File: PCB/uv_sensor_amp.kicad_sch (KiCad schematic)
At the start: 4 parts, among them U2 LMV321

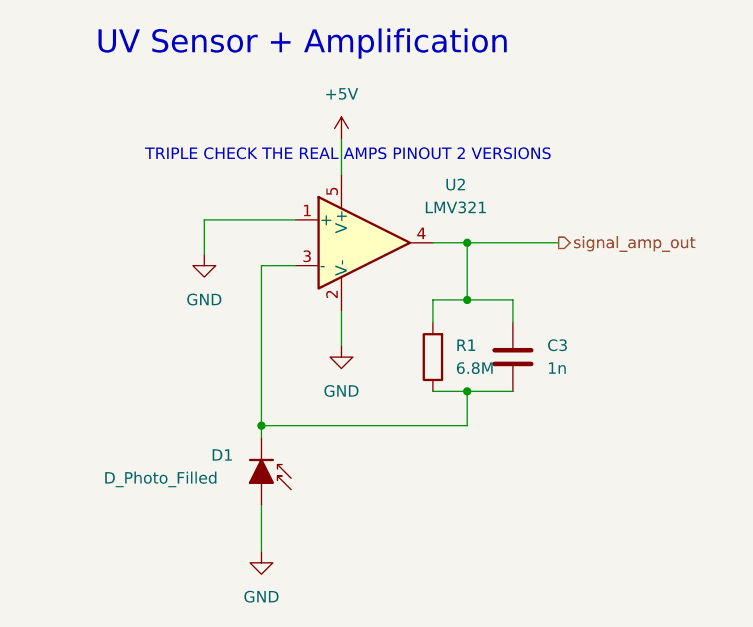
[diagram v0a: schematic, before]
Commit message: add footprints for power supply
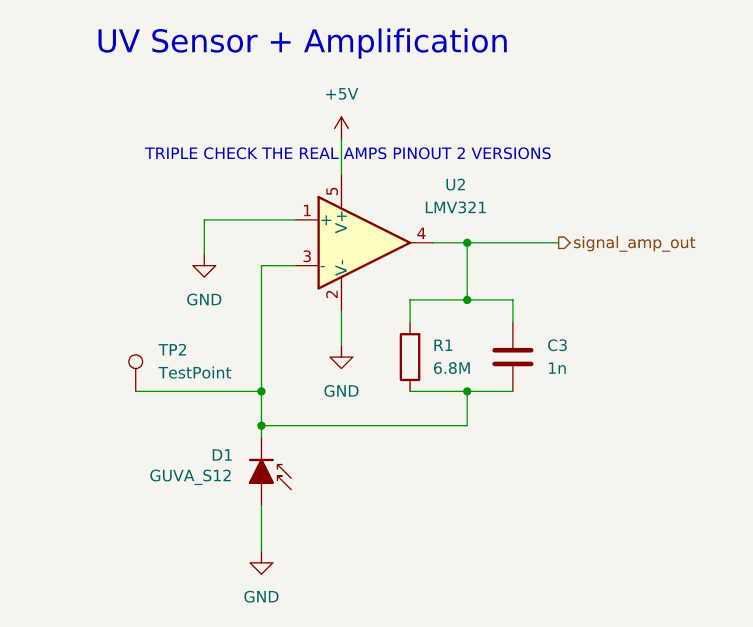
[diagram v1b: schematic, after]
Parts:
- added TP2: TestPoint, TestPoint:TestPoint_Keystone_5000-5004_Miniature, symbol Connector:TestPoint
- D1: value D_Photo_Filled -> GUVA_S12
- R1: footprint Resistor_SMD:R_0402_1005Metric -> Resistor_SMD:R_0805_2012Metric_Pad1.20x1.40mm_HandSolder
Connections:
- net at C3.2, D1.1 (K), R1.1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: now also TP2.1
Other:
- moved on the sheet: R1
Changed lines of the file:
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@@
 		(color 0 0 0 0)
 	)
+	(junction
+		(at 113.03 92.71)
+		(diameter 0)
+		(color 0 0 0 0)
+	)
 	(wire
 		(pts
@@
 	(wire
 		(pts
+			(xy 99.06 92.71) (xy 113.03 92.71)
+		)
+		(stroke
+			(width 0)
+			(type default)
+		)
+	)
+	(wire
+		(pts
 			(xy 106.68 73.66) (xy 106.68 77.47)
 		)
@@
 	(wire
 		(pts
-			(xy 113.03 96.52) (xy 113.03 78.74)
-		)
-		(stroke
-			(width 0)
-			(type default)
-		)
-	)
-	(wire
-		(pts
 			(xy 135.89 76.2) (xy 135.89 82.55)
 		)
@@
 	(wire
 		(pts
-			(xy 132.08 92.71) (xy 135.89 92.71)
-		)
-		(stroke
-			(width 0)
-			(type default)
-		)
-	)
-	(wire
-		(pts
-			(xy 135.89 82.55) (xy 132.08 82.55)
+			(xy 129.54 92.71) (xy 135.89 92.71)
+		)
+		(stroke
+			(width 0)
+			(type default)
+		)
+	)
+	(wire
+		(pts
+			(xy 135.89 82.55) (xy 129.54 82.55)
+		)
+		(stroke
+			(width 0)
+			(type default)
+		)
+	)
+	(wire
+		(pts
+			(xy 113.03 78.74) (xy 113.03 92.71)
+		)
+		(stroke
+			(width 0)
+			(type default)
+		)
+	)
+	(wire
+		(pts
+			(xy 113.03 92.71) (xy 113.03 96.52)
 		)
 		(stroke
@@
 	(wire
 		(pts
-			(xy 132.08 82.55) (xy 132.08 85.09)
+			(xy 129.54 82.55) (xy 129.54 85.09)
 		)
 		(stroke
@@
 			)
 			(justify left)
+		)
+	)
+	(symbol
+		(lib_id "Connector:TestPoint")
+		(at 99.06 92.71 0)
+		(unit 1)
+		(body_style 1)
+		(exclude_from_sim no)
+		(in_bom yes)
+		(on_board yes)
+		(in_pos_files yes)
+		(dnp no)
+		(fields_autoplaced yes)
+		(property "Reference" "TP2"
+			(at 101.6 88.1379 0)
+			(show_name no)
+			(do_not_autoplace no)
+			(effects
+				(font
+					(size 1.27 1.27)
+				)
+				(justify left)
+			)
+		)
+		(property "Value" "TestPoint"
+			(at 101.6 90.6779 0)
+			(show_name no)
+			(do_not_autoplace no)
+			(effects
+				(font
+					(size 1.27 1.27)
+				)
+				(justify left)
+			)
+		)
+		(property "Footprint" "TestPoint:TestPoint_Keystone_5000-5004_Miniature"
+			(at 104.14 92.71 0)
+			(hide yes)
+			(show_name no)
+			(do_not_autoplace no)
+			(effects
+				(font
+					(size 1.27 1.27)
+				)
+			)
+		)
+		(property "Datasheet" ""
+			(at 104.14 92.71 0)
+			(hide yes)
+			(show_name no)
+			(do_not_autoplace no)
+			(effects
+				(font
+					(size 1.27 1.27)
+				)
+			)
+		)
+		(property "Description" "test point"
+			(at 99.06 92.71 0)
+			(hide yes)
+			(show_name no)
+			(do_not_autoplace no)
+			(effects
+				(font
+					(size 1.27 1.27)
+				)
+			)
+		)
+		(pin "1"
+		)
+		(instances
+			(project "UV_badge"
+				(path "/510c3167-274e-48e8-bc0f-ce517acc7f9d/ab3e44bd-2a8b-4d5e-afa5-e8b03dc741f3"
+					(reference "TP2")
+					(unit 1)
+				)
+			)
 		)
 	)
@@
 			)
 		)
-		(property "Value" "D_Photo_Filled"
-			(at 95.504 102.362 90)
+		(property "Value" "GUVA_S12"
+			(at 100.584 102.108 90)
 			(show_name no)
 			(do_not_autoplace no)
@@
 	(symbol
 		(lib_id "Device:R")
-		(at 132.08 88.9 180)
+		(at 129.54 88.9 180)
 		(unit 1)
 		(body_style 1)
@@
 		(fields_autoplaced yes)
 		(property "Reference" "R1"
-			(at 134.62 87.6299 0)
+			(at 132.08 87.6299 0)
 			(show_name no)
 			(do_not_autoplace no)
@@
 		)
 		(property "Value" "6.8M"
-			(at 134.62 90.1699 0)
+			(at 132.08 90.1699 0)
 			(show_name no)
 			(do_not_autoplace no)
@@
 			)
 		)
-		(property "Footprint" "Resistor_SMD:R_0402_1005Metric"
-			(at 133.858 88.9 90)
+		(property "Footprint" "Resistor_SMD:R_0805_2012Metric_Pad1.20x1.40mm_HandSolder"
+			(at 131.318 88.9 90)
 			(hide yes)
 			(show_name no)
@@
 		)
 		(property "Datasheet" ""
-			(at 132.08 88.9 0)
+			(at 129.54 88.9 0)
 			(hide yes)
 			(show_name no)
@@
 		)
 		(property "Description" "Resistor"
-			(at 132.08 88.9 0)
-			(hide yes)
-			(show_name no)
+			(at 129.54 88.9 0)
+			(hide yes)
+			(show_name no)

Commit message: add missing symbols
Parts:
- U2: footprint Package_TO_SOT_SMD:SOT-23-5 -> Package_TO_SOT_SMD:SOT-23-5_HandSoldering
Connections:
- net GND: now also U2.3 (+); no longer U2.1 (+)
- net signal_amp_out: now also U2.1; no longer U2.4
- net at C3.2, D1.1 (K), R1.1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: now also U2.4 (-); no longer U2.3 (-)
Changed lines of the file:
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@@
 			)
 		)
-		(property "Footprint" "Package_TO_SOT_SMD:SOT-23-5"
+		(property "Footprint" "Package_TO_SOT_SMD:SOT-23-5_HandSoldering"
 			(at 124.46 76.2 0)
 			(hide yes)
@@
 			)
 		)
-		(property "Description" "Low-Voltage Rail-to-Rail Output Operational Amplifiers, SOT-23-5/SC-70-5"
+		(property "Description" "https://www.tme.eu/de/details/lmv321aidbvr/smd-operationsverstaerker/texas-instruments/"
 			(at 124.46 76.2 0)
 			(hide yes)

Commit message: update LED footprint reverse mount
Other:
- note removed: "TRIPLE CHECK THE REAL AMPS PINOUT 2 VERSIONS"
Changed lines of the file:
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@@
 	(generator_version "10.0")
 	(paper "A4")
-	(text "TRIPLE CHECK THE REAL AMPS PINOUT 2 VERSIONS"
-		(exclude_from_sim no)
-		(at 122.682 66.548 0)
-		(effects
-			(font
-				(size 1.27 1.27)
-			)
-		)
-	)
 	(text "UV Sensor + Amplification\n"
 		(exclude_from_sim no)
